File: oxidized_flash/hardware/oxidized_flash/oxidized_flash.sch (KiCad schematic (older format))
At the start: 35 parts, among them J1 USB_B_Micro, U1 LM1117-3.3, U2 ATSAMD51G18A-MU, U3 IS21ES

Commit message: Add power LED
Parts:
- added D4: PWR_LED, LED_SMD:LED_0805_2012Metric, symbol Device:LED_Small
- added R8: 1k, Resistor_SMD:R_0805_2012Metric, symbol Device:R_Small
- D1: value LED_Small -> OK_Led
- R2: value 10k -> 1k
- R9: renamed from R?; footprint (none) -> Resistor_SMD:R_0805_2012Metric
- gave numbers to parts that had none: 1
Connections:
- net +3V3: now also D4.2 (A), R8.2
- new net: D4.1 (K), R8.1
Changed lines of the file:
@@
 P 2200 3050
 F 0 "R2" H 2259 3096 50  0000 L CNN
-F 1 "10k" H 2259 3005 50  0000 L CNN
+F 1 "1k" H 2259 3005 50  0000 L CNN
 F 2 "Resistor_SMD:R_0805_2012Metric" H 2200 3050 50  0001 C CNN
 F 3 "~" H 2200 3050 50  0001 C CNN
@@
 P 1050 4150
 F 0 "D1" V 1096 4082 50  0000 R CNN
-F 1 "LED_Small" V 1005 4082 50  0000 R CNN
+F 1 "OK_Led" V 1005 4082 50  0000 R CNN
 F 2 "LED_SMD:LED_0805_2012Metric" V 1050 4150 50  0001 C CNN
 F 3 "~" V 1050 4150 50  0001 C CNN
@@
 NoConn ~ 6750 2350
 $Comp
-L Connector:Conn_ARM_JTAG_SWD_10 J?
+L Connector:Conn_ARM_JTAG_SWD_10 J2
 U 1 1 5C6F27D1
 P 2100 6000
-F 0 "J?" H 1657 6046 50  0000 R CNN
+F 0 "J2" H 1657 6046 50  0000 R CNN
 F 1 "Conn_ARM_JTAG_SWD_10" H 1657 5955 50  0000 R CNN
 F 2 "Connector_PinHeader_1.27mm:PinHeader_2x05_P1.27mm_Vertical_SMD" H 2150 5450 50  0001 L TNN
@@
 	2100 6700 2100 6600
 $Comp
-L power:GND #PWR?
+L power:GND #PWR0101
 U 1 1 5C6FEFCE
 P 2100 6800
-F 0 "#PWR?" H 2100 6550 50  0001 C CNN
+F 0 "#PWR0101" H 2100 6550 50  0001 C CNN
 F 1 "GND" H 2105 6627 50  0000 C CNN
 F 2 "" H 2100 6800 50  0001 C CNN
@@
 	2100 5400 2100 5300
 $Comp
-L power:+3.3V #PWR?
+L power:+3.3V #PWR0102
 U 1 1 5C747FA9
 P 2100 5300
-F 0 "#PWR?" H 2100 5150 50  0001 C CNN
+F 0 "#PWR0102" H 2100 5150 50  0001 C CNN
 F 1 "+3.3V" H 2115 5473 50  0000 C CNN
 F 2 "" H 2100 5300 50  0001 C CNN
@@
 SWD_CLK
 $Comp
-L Device:R_Small R?
+L Device:R_Small R9
 U 1 1 5C752F56
 P 2400 3950
-F 0 "R?" H 2459 3996 50  0000 L CNN
+F 0 "R9" H 2459 3996 50  0000 L CNN
 F 1 "10k" H 2459 3905 50  0000 L CNN
-F 2 "" H 2400 3950 50  0001 C CNN
+F 2 "Resistor_SMD:R_0805_2012Metric" H 2400 3950 50  0001 C CNN
 F 3 "~" H 2400 3950 50  0001 C CNN
 	1    2400 3950
@@
 	2400 3850 2400 3800
 $Comp
-L power:+3.3V #PWR?
+L power:+3.3V #PWR0103
 U 1 1 5C770522
 P 2400 3800
-F 0 "#PWR?" H 2400 3650 50  0001 C CNN
+F 0 "#PWR0103" H 2400 3650 50  0001 C CNN
 F 1 "+3.3V" H 2415 3973 50  0000 C CNN
 F 2 "" H 2400 3800 50  0001 C CNN
@@
 Text Label 1850 3200 0    50   ~ 0
 SWD_RST
+$Comp
+L Device:LED_Small D4
+U 1 1 5C791600
+P 1550 4150
+F 0 "D4" V 1596 4082 50  0000 R CNN
+F 1 "PWR_LED" V 1505 4082 50  0000 R CNN
+F 2 "LED_SMD:LED_0805_2012Metric" V 1550 4150 50  0001 C CNN
+F 3 "~" V 1550 4150 50  0001 C CNN
+	1    1550 4150
+	0    -1   -1   0
+$EndComp
+$Comp
+L power:+3.3V #PWR0104
+U 1 1 5C7A5007
+P 1550 3900
+F 0 "#PWR0104" H 1550 3750 50  0001 C CNN
+F 1 "+3.3V" H 1565 4073 50  0000 C CNN
+F 2 "" H 1550 3900 50  0001 C CNN
+F 3 "" H 1550 3900 50  0001 C CNN
+	1    1550 3900
+	1    0    0    -1
+$EndComp
+Wire Wire Line
+	1550 4050 1550 3900
+$Comp
+L Device:R_Small R8
+U 1 1 5C7AE489
+P 1550 4450
+F 0 "R8" H 1609 4496 50  0000 L CNN
+F 1 "1k" H 1609 4405 50  0000 L CNN
+F 2 "Resistor_SMD:R_0805_2012Metric" H 1550 4450 50  0001 C CNN
+F 3 "~" H 1550 4450 50  0001 C CNN
+	1    1550 4450
+	1    0    0    -1
+$EndComp
+Wire Wire Line
+	1550 4350 1550 4250
+Wire Wire Line
+	1550 4550 1550 4700
+$Comp
+L power:GND #PWR0105
+U 1 1 5C7C0C91
+P 1550 4700
+F 0 "#PWR0105" H 1550 4450 50  0001 C CNN
+F 1 "GND" H 1555 4527 50  0000 C CNN
+F 2 "" H 1550 4700 50  0001 C CNN
+F 3 "" H 1550 4700 50  0001 C CNN
+	1    1550 4700
+	1    0    0    -1
+$EndComp
 $EndSCHEMATC

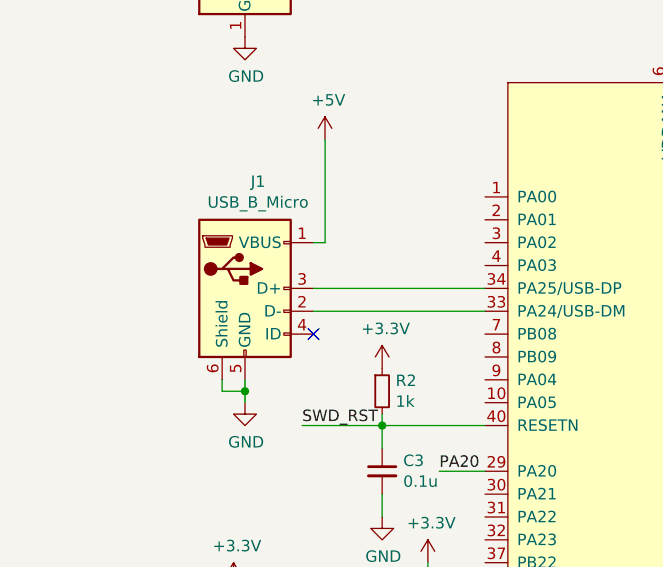
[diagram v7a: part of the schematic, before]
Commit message: Add Molex USB type A footprint
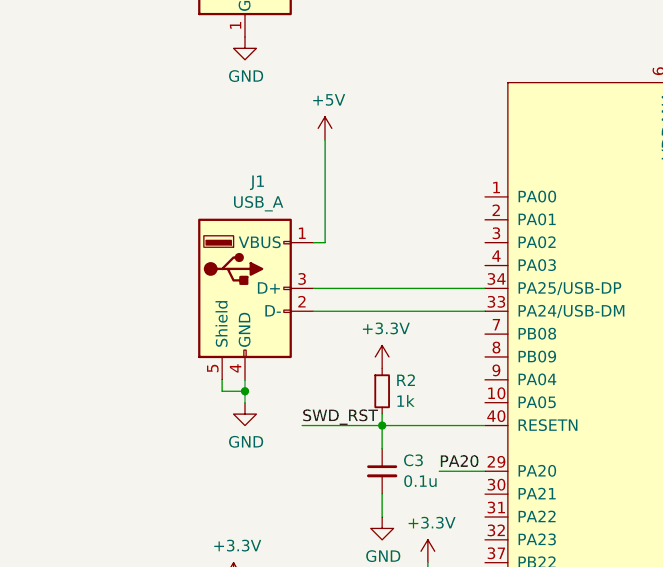
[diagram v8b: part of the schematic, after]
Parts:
- removed J1: USB_B_Micro, Custom_USB:USB-MICRO-B-FCI-10118192, symbol Connector:USB_B_Micro
- added J1: USB_A, Custom_USB:Molex_48037_USB_A_Male, symbol Connector:USB_A
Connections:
- net +3V3: now also J1.4 (GND), J1.5 (Shield)
- net +5V: now also J1.1 (VBUS)
- net at U2.33 (PA24/USB-DM): now also J1.2 (D-)
- net at U2.34 (PA25/USB-DP): now also J1.3 (D+)
- no-connect marks 11 -> 10
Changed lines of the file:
@@
 	1    0    0    -1
 $EndComp
-NoConn ~ 1900 2800
 Wire Wire Line
 	4400 3600 4500 3600
@@
 F 3 "" H 5450 5200 50  0001 C CNN
 	1    5450 5200
-	1    0    0    -1
-$EndComp
-$Comp
-L Connector:USB_B_Micro J1
-U 1 1 5C43966C
-P 1600 2600
-F 0 "J1" H 1657 3067 50  0000 C CNN
-F 1 "USB_B_Micro" H 1657 2976 50  0000 C CNN
-F 2 "Custom_USB:USB-MICRO-B-FCI-10118192" H 1750 2550 50  0001 C CNN
-F 3 "~" H 1750 2550 50  0001 C CNN
-	1    1600 2600
 	1    0    0    -1
 $EndComp
@@
 	1    0    0    -1
 $EndComp
+$Comp
+L Connector:USB_A J1
+U 1 1 5C7CB7A2
+P 1600 2600
+F 0 "J1" H 1657 3067 50  0000 C CNN
+F 1 "USB_A" H 1657 2976 50  0000 C CNN
+F 2 "Custom_USB:Molex_48037_USB_A_Male" H 1750 2550 50  0001 C CNN
+F 3 " ~" H 1750 2550 50  0001 C CNN
+	1    1600 2600
+	1    0    0    -1
+$EndComp
